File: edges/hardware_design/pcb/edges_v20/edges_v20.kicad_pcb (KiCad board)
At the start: 2 copper layers, 97.8 x 102.9 mm, 179 parts, among them IC1 LM4041DBZ, IC10 TL072D, IC11 LM4041DBZ, IC12 TL072D, IC13 MCP3208, IC14 REG1117, IC15 MCP4822SO08, IC16 AVR_XMEGA_A4_44A, IC2 TL072D, IC3 TL072D, IC4 TL072D, IC5 741G125DBV, IC6 741G86DBV, IC7 TL072D, IC8 741G86DBV, IC9 TL072D, J1 PJ301_THONKICONN6, J10 PJ301_THONKICONN6, J11 PJ301_THONKICONN6, J12 PJ301_THONKICONN6, J13 PJ301_THONKICONN6, J14 PJ301_THONKICONN6, J15 PJ301_THONKICONN6, J16 PJ301_THONKICONN6, J17 PJ301_THONKICONN6, J18 AVR_SPI_PRG_6PTH, J19 M05X2PTH, J2 PJ301_THONKICONN6, J20 AVR_SPI_PRG_6PTH, J3 PJ301_THONKICONN6, J4 PJ301_THONKICONN6, J5 PJ301_THONKICONN6, J6 PJ301_THONKICONN6, J7 PJ301_THONKICONN6, J8 PJ301_THONKICONN6, J9 PJ301_THONKICONN6, Q1 MMBT3904, Q2 MMBT3904, Q3 MMBT3904, Q4 MMBT3904, Q5 8MHz, SW1 S-ON-ONSMALL_SLIDE, SW2 S-ON-ONSMALL_SLIDE, SW3 S-ON-ONSMALL_SLIDE, SW4 TAC_SWITCHPTH, SW5 TAC_SWITCHPTH, SW6 TAC_SWITCHPTH, SW7 TAC_SWITCHPTH

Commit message: refined edges kicad
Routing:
- net +3V3: track 463.0 -> 477.9 mm
- net Net-(IC16-AVCC): track 17.8 -> 26.2 mm
- net /edges_v20_2/CV2: track 43.5 -> 48.8 mm
- net CH3: track 60.8 -> 63.8 mm
- net /edges_v20_2/FM4: track 5.82 -> 7.93 mm
- net CH8: track 35.6 -> 37.5 mm
- net AREF_-10: track 182.9 -> 184.1 mm
- net /edges_v20_1/GATE3: track 87.0 -> 86.5 mm
- net GND: vias 103 -> 104
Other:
- board text added: "3.3V MIDIin GND"
- board text added: "LEARN NEStri MODE"
- board text added: "production run 2023 @mb"

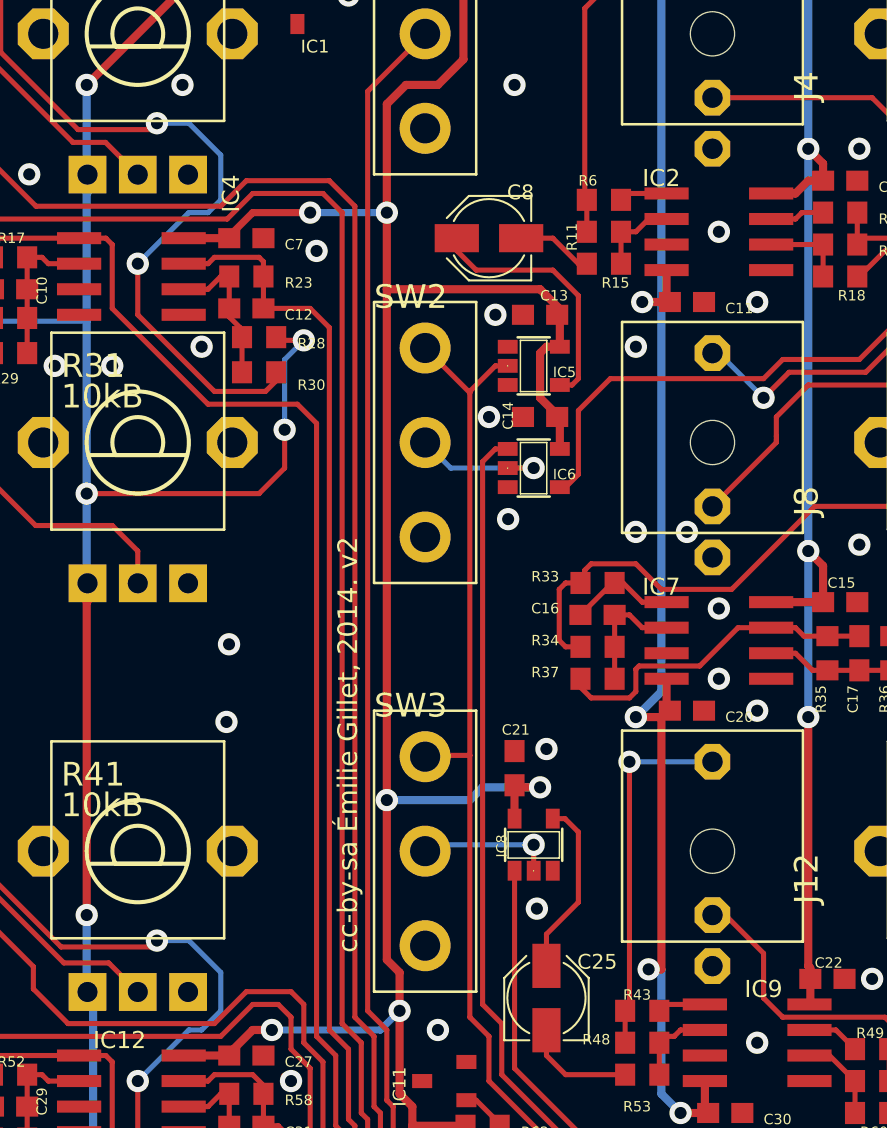
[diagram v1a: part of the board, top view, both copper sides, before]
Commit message: Edges pcb optimzed a little
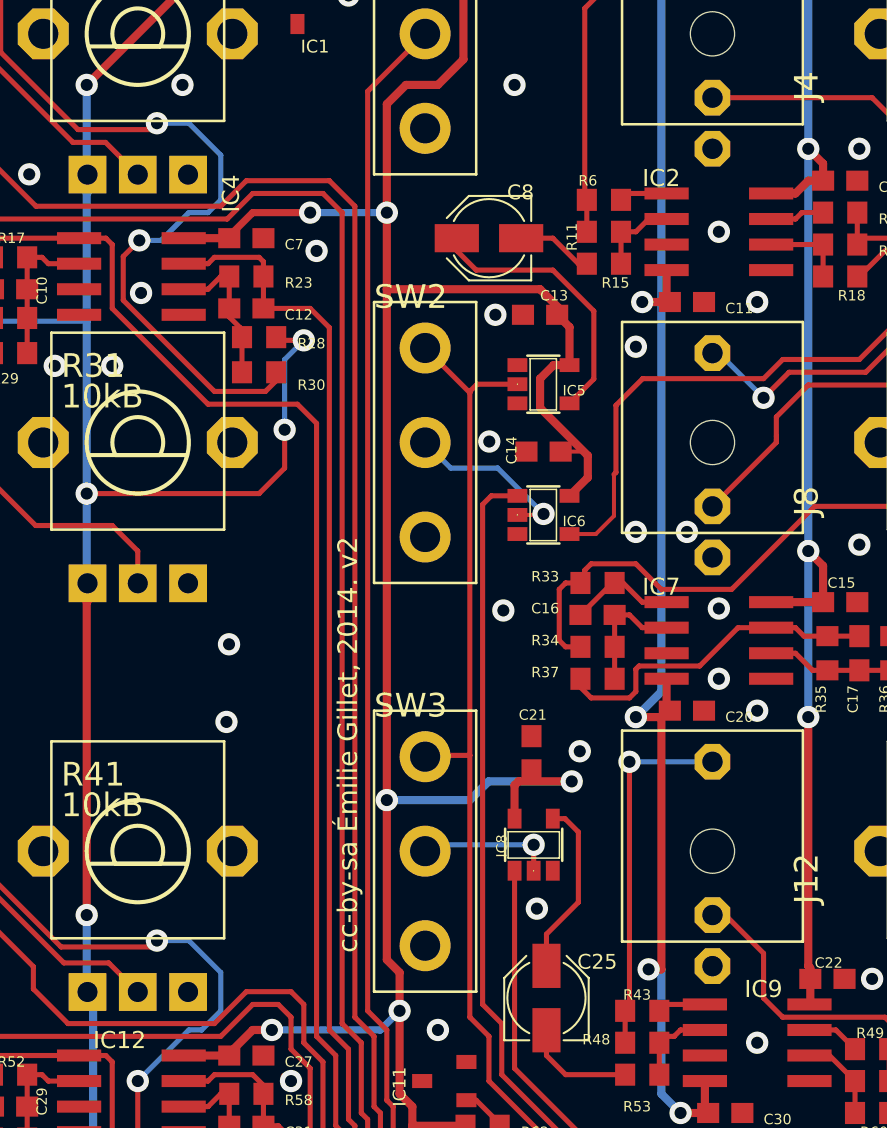
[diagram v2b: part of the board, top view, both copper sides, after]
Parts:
- moved IC6 2.38 mm to (167.1, 87.7)
- moved C14 1.73 mm to (167.1, 84.5)
- moved C21 1.12 mm to (166.5, 99.5)
- moved IC5 1.03 mm to (167.1, 81.2)
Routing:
- net +3V3: track 477.9 -> 486.4 mm
- net CHANNEL2: track 24.8 -> 26.6 mm
- net Net-(IC16-PC4): track 81.5 -> 79.8 mm
- net Net-(IC6A-I1): track 7.21 -> 8.68 mm
- net /edges_v20_2/FM1: track 44.2 -> 45.4 mm
- net CHANNEL1: track 12.8 -> 13.8 mm
